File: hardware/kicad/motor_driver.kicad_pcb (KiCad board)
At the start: 2 copper layers, 44.9 x 47.2 mm, 18 parts, among them J1 5V_ADAPTER, J2 5V_IN, J3 TO_MOTOR, J4 FROM_MCU, U1 ULN2003A

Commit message: docs: added pcb export - buck_3V3
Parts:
- moved G*** 4.28 mm to (83.0, 83.3)
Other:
- board size 44.9 x 47.2 mm -> 44.9 x 52 mm
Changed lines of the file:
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@@
+      (rotate (xyz 0 0 0))
+    )
+    (model ":KICAD7_3DMODEL_DIR:Connector_BarrelJack.3dshapes/BarrelJack_GCT_DCJ200-10-A_Horizontal.step"
+      (offset (xyz 0 0 0))
+      (scale (xyz 1 1 1))
       (rotate (xyz 0 0 0))
     )
   )
   (footprint "Logo:logo_pcb" (layer "F.Cu")
-    (at 82.75 79)
+    (at 83 83.275)
     (attr board_only exclude_from_pos_files exclude_from_bom)
     (fp_text reference "G***" (at -4.25 0) (layer "F.SilkS") hide
@@
     )
   )
-  (gr_rect (start 76.2 34.77) (end 121.09 81.97)
+  (gr_rect (start 76.2 34.77) (end 121.09 86.77)
     (stroke (width 0.05) (type default)) (fill none) (layer "Edge.Cuts"))
   (gr_text "5V" (at 77 54.5) (layer "F.SilkS")
@@
     (effects (font (size 1 1) (thickness 0.1)) (justify left bottom))
   )
-  (gr_text "Fyosa-Elec\nBoard V1.0" (at 86.25 80.25) (layer "F.SilkS")
+  (gr_text "Fyosa-Elec\nBoard V1.0" (at 85.975 84.475) (layer "F.SilkS")
     (effects (font (size 1 1) (thickness 0.2) bold) (justify left bottom))
   )
@@
     (effects (font (size 1 1) (thickness 0.1)) (justify left bottom))
   )
-  (gr_text "Min. V: 5V\nMin. I: 1A" (at 109.25 81.25) (layer "F.SilkS")
+  (gr_text "Min. V: 5V\nMin. I: 1A" (at 109.75 84.825) (layer "F.SilkS")
     (effects (font (size 1 1) (thickness 0.1)) (justify left bottom))
   )
@@
       (pts
         (xy 76.2 34.8)
-        (xy 76.2 82)
-        (xy 121.1 81.95)
+        (xy 76.175 86.625)
+        (xy 121.075 86.575)
         (xy 121.05 34.8)
       )

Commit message: fix: smd packages for reverse polarity & board orientation
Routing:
- net /GND: vias 5 -> 1
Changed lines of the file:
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@@
   (segment (start 106.367677 64) (end 106.35 64) (width 0.8) (layer "F.Cu") (net 1))
   (segment (start 118.55 50.7) (end 113.26 55.99) (width 0.8) (layer "F.Cu") (net 1))
-  (via (at 105.75 61.4) (size 0.6) (drill 0.3) (layers "F.Cu" "B.Cu") (free) (net 2))
-  (via (at 105.5 74.65) (size 0.6) (drill 0.3) (layers "F.Cu" "B.Cu") (free) (net 2))
   (via (at 111.9 61.4) (size 0.6) (drill 0.3) (layers "F.Cu" "B.Cu") (free) (net 2))
-  (via (at 102.35 61.4) (size 0.6) (drill 0.3) (layers "F.Cu" "B.Cu") (free) (net 2))
-  (via (at 106.8 79.95) (size 0.6) (drill 0.3) (layers "F.Cu" "B.Cu") (free) (net 2))
   (segment (start 78.75 64) (end 81 66.25) (width 0.8) (layer "F.Cu") (net 3))
   (segment (start 79.7 54.25) (end 78.75 55.2) (width 0.8) (layer "F.Cu") (net 3))

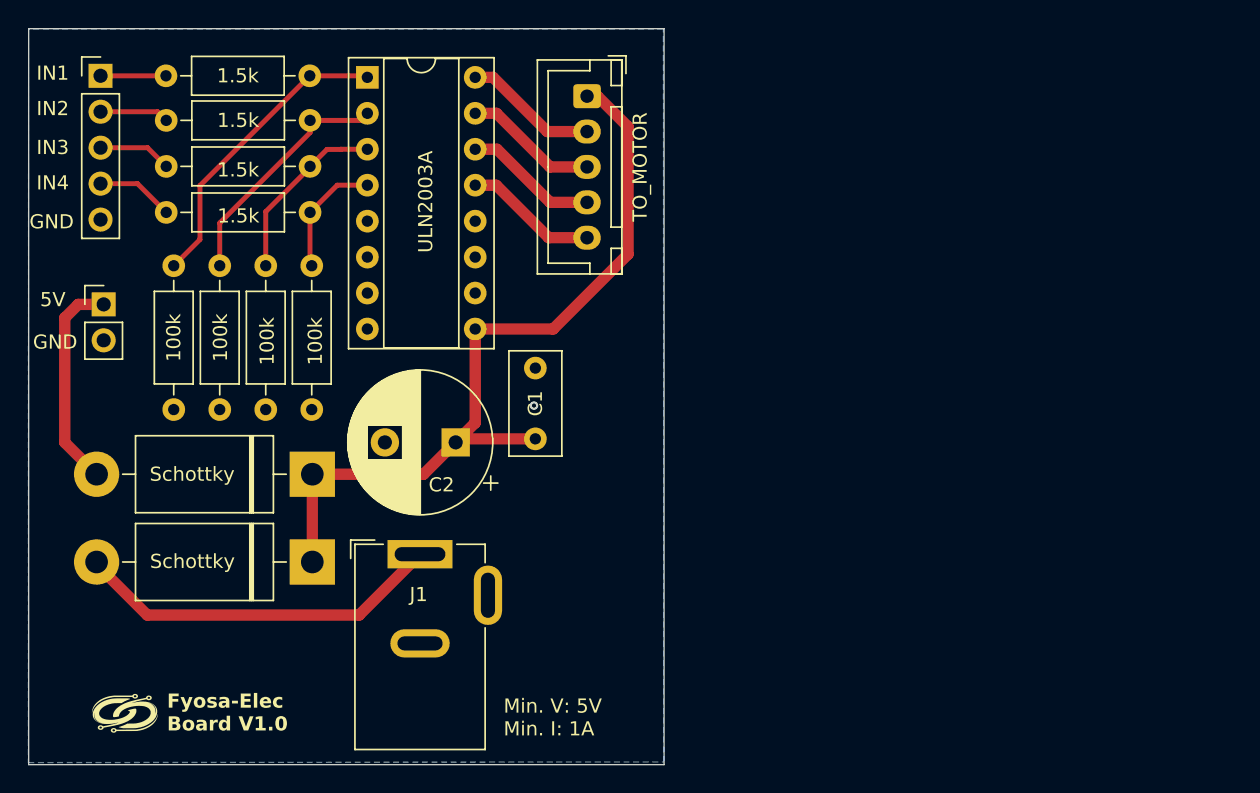
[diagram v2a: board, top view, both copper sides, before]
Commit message: fix: 3d, pcb & packages - motor driver
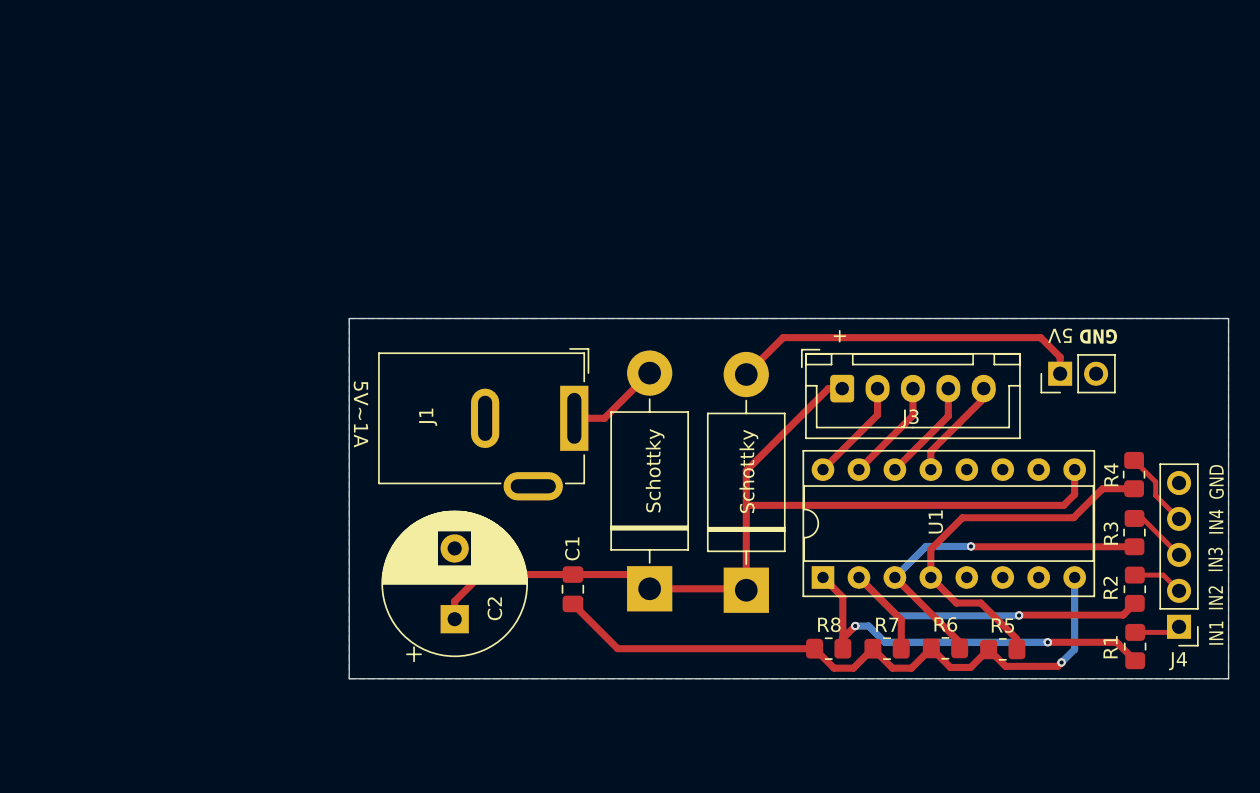
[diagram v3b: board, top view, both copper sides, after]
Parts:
- removed G***: LOGO, Logo:logo_pcb
- C1: footprint Capacitor_THT:C_Rect_L7.2mm_W3.5mm_P5.00mm_FKS2_FKP2_MKS2_MKP2 -> Capacitor_SMD:C_0805_2012Metric_Pad1.18x1.45mm_HandSolder
- R1, R2, R4, R5, R6, R7, R8: footprint Resistor_THT:R_Axial_DIN0207_L6.3mm_D2.5mm_P10.16mm_Horizontal -> Resistor_SMD:R_0805_2012Metric_Pad1.20x1.40mm_HandSolder
- R3: value 1.5k -> 1,5k; footprint Resistor_THT:R_Axial_DIN0207_L6.3mm_D2.5mm_P10.16mm_Horizontal -> Resistor_SMD:R_0805_2012Metric_Pad1.20x1.40mm_HandSolder
- moved J4 85.6 mm to (157.5, 77.0), turned to 180 degrees
- moved R1 79.5 mm to (154.4, 78.4), turned to -90 degrees
- moved R2 76.0 mm to (154.3, 74.4), turned to -90 degrees
- moved R3 73.1 mm to (154.3, 70.4), turned to -90 degrees
- moved R4 70.8 mm to (154.3, 66.3), turned to -90 degrees
- moved J2 67.8 mm to (149.1, 59.1), turned to 90 degrees
- moved R5 51.7 mm to (145.0, 78.6), turned to 0 degrees
- moved R6 50.9 mm to (141.0, 78.5), turned to 0 degrees
- moved R7 50.1 mm to (136.8, 78.6), turned to 0 degrees
- moved R8 49.3 mm to (132.7, 78.6), turned to 0 degrees
- moved U1 47.8 mm to (132.3, 73.5), turned to 90 degrees
- moved D1 31.7 mm to (126.9, 74.4), turned to 90 degrees
- moved J3 27.4 mm to (133.7, 60.2), turned to 0 degrees
- moved D2 23.9 mm to (120.1, 74.3), turned to 90 degrees
- moved J1 14.5 mm to (114.8, 62.3), turned to -90 degrees
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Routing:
- net /GND: track 0.00 -> 46.2 mm
- net Net-(D2-A): track 26.3 -> 6.65 mm
- net Net-(U1-I4): track 8.66 -> 26.7 mm
- net Net-(U1-I3): track 12.9 -> 24.7 mm, vias 0 -> 1
- net Net-(U1-I2): track 17.2 -> 27.2 mm, vias 0 -> 1
- net Net-(D1-A): track 15.1 -> 25.0 mm
- net Net-(D1-K): track 57.5 -> 66.0 mm
- net Net-(U1-I1): track 21.5 -> 28.4 mm, vias 0 -> 2
- net Net-(J3-Pin_3): track 9.47 -> 7.31 mm
- net Net-(J3-Pin_4): track 9.45 -> 7.29 mm
- net Net-(J3-Pin_5): track 9.44 -> 7.27 mm
- net Net-(J3-Pin_2): track 9.49 -> 7.32 mm
- net Net-(J4-Pin_1): track 4.62 -> 3.26 mm
- net Net-(J4-Pin_2): track 4.89 -> 3.59 mm
- net Net-(J4-Pin_3): track 5.19 -> 4.22 mm
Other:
- board size 44.9 x 52 mm -> 62.1 x 25.5 mm
- board text added: "+"
- board text added: "5V~1A"
- board text removed: "Fyosa-Elec Board V1.0"
- board text removed: "Min. V: 5V Min. I: 1A"
